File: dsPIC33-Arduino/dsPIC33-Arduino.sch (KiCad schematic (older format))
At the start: 58 parts, among them CON1 BARREL_JACK, P1 Power, P10 PIN20, P11 PIN5, P12 PWR_IN, P13 PIN2, P14 Power Select, P15 I2C, P16 PIN19, P17 UART, P2 Analog, P3 Digital, P4 Digital, P5 CONN_1, P6 CONN_1, P7 CONN_1, P8 CONN_1, P9 USB_B, SW1 SW_PUSH, U1 FT230XS, U2 LM1117 3V3, U3 dsPIC33EVxxxGM102-I/SP, U4 74LVC1G32, U5 7805, Y1 Crystal

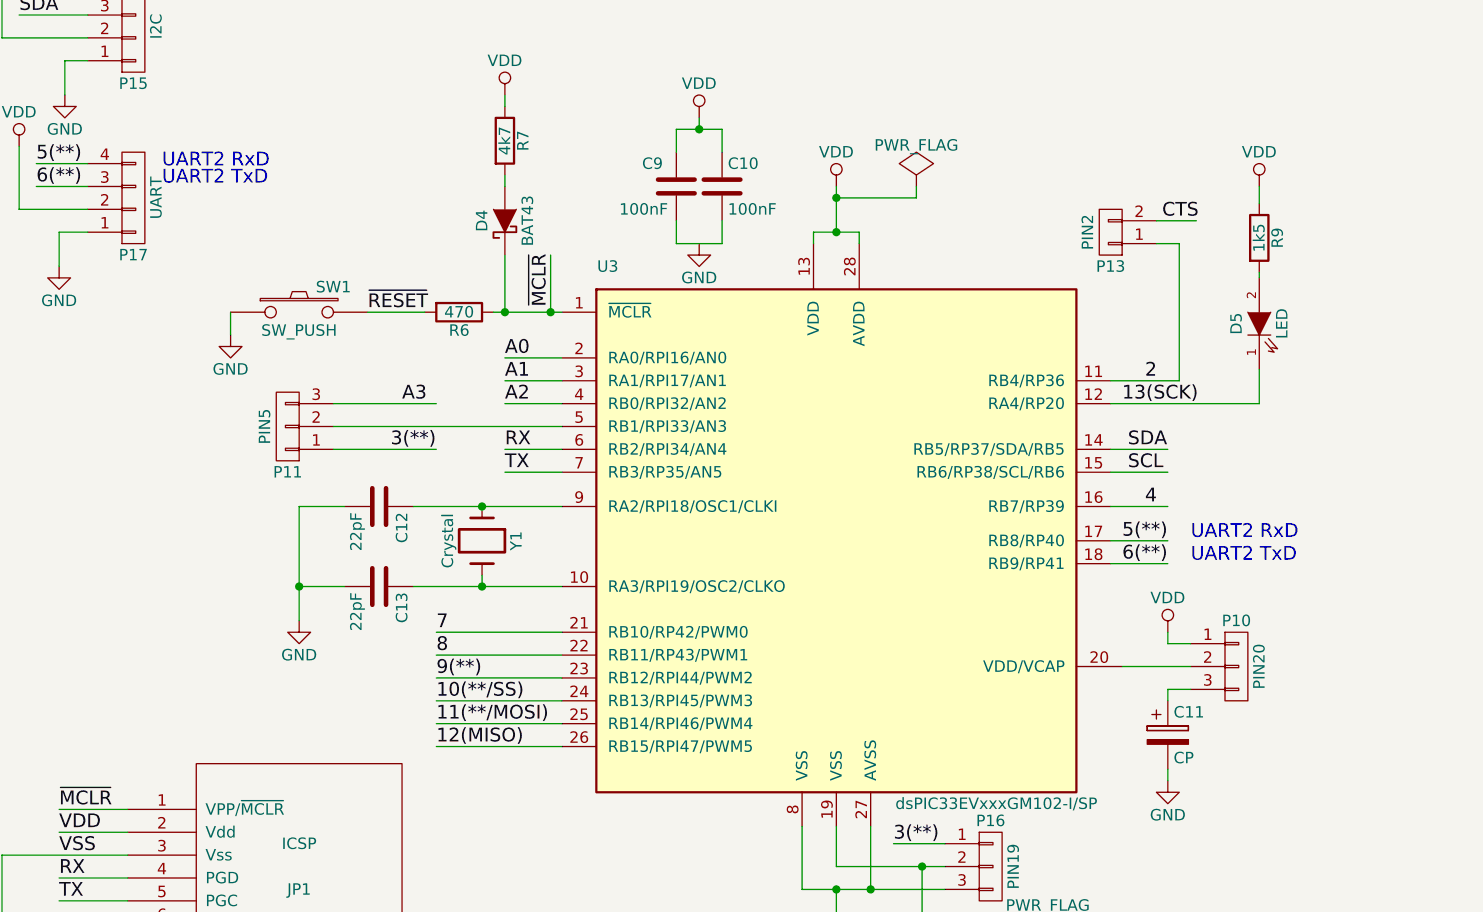
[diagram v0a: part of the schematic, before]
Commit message: use diode the right way
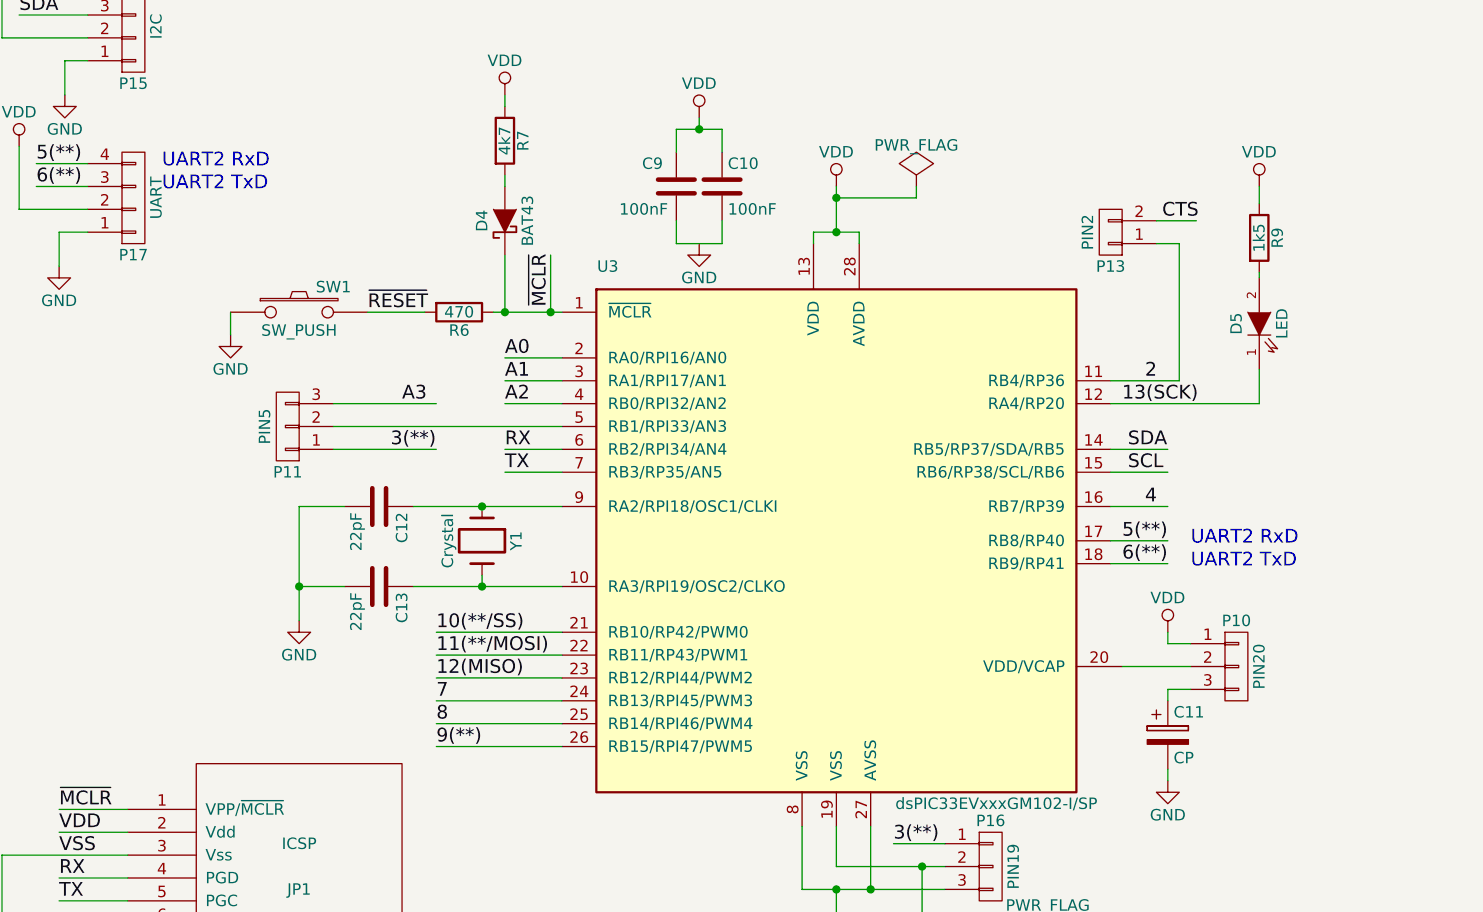
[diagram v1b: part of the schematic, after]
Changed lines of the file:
@@
 Text Label 5550 5800 0    60   ~ 0
 5(**)
+Text Label 2550 6500 0    60   ~ 0
+7
+Text Label 2550 6600 0    60   ~ 0
+8
+Text Label 2550 6700 0    60   ~ 0
+9(**)
 Text Label 2550 6200 0    60   ~ 0
-7
+10(**/SS)
 Text Label 2550 6300 0    60   ~ 0
-8
+11(**/MOSI)
 Text Label 2550 6400 0    60   ~ 0
-9(**)
-Text Label 2550 6500 0    60   ~ 0
-10(**/SS)
-Text Label 2550 6600 0    60   ~ 0
-11(**/MOSI)
-Text Label 2550 6700 0    60   ~ 0
 12(MISO)
 $Comp
@@
 	0    -1   -1   0
 $EndComp
-Text Notes 5850 5900 0    60   ~ 0
+Text Notes 5850 5925 0    60   ~ 0
 UART2 TxD
-Text Notes 5850 5800 0    60   ~ 0
+Text Notes 5850 5825 0    60   ~ 0
 UART2 RxD
-Text Notes 1350 4250 0    60   ~ 0
+Text Notes 1350 4275 0    60   ~ 0
 UART2 TxD
 Text Notes 1350 4175 0    60   ~ 0

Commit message: wip
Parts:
- removed C14, C15, C7: 100nF, Capacitors_ThroughHole:C_Disc_D3_P2.5, symbol C
- added C14, C15, C7: 47uF, w_capacitors:CP_4x5mm, symbol CP
- C11: value CP -> 10uF ESR
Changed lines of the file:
@@
-$EndComp
-$Comp
-L C C7
-U 1 1 588D100F
-P 5650 2700
-F 0 "C7" H 5675 2800 50  0000 L CNN
-F 1 "100nF" H 5675 2600 50  0000 L CNN
-F 2 "Capacitors_ThroughHole:C_Disc_D3_P2.5" H 5688 2550 50  0001 C CNN
-F 3 "" H 5650 2700 50  0000 C CNN
-	1    5650 2700
-	1    0    0    -1
 $EndComp
 $Comp
@@
 P 5750 6650
 F 0 "C11" H 5775 6750 50  0000 L CNN
-F 1 "CP" H 5775 6550 50  0000 L CNN
+F 1 "10uF ESR" H 5775 6550 50  0000 L CNN
 F 2 "w_capacitors:CP_4x5mm" H 5788 6500 50  0001 C CNN
 F 3 "" H 5750 6650 50  0000 C CNN
@@
 F 3 "" H 6100 1850 50  0000 C CNN
 	1    6100 1850
-	1    0    0    -1
-$EndComp
-$Comp
-L C C14
-U 1 1 588E4312
-P 5650 1550
-F 0 "C14" H 5675 1650 50  0000 L CNN
-F 1 "100nF" H 5675 1450 50  0000 L CNN
-F 2 "Capacitors_ThroughHole:C_Disc_D3_P2.5" H 5688 1400 50  0001 C CNN
-F 3 "" H 5650 1550 50  0000 C CNN
-	1    5650 1550
-	1    0    0    -1
-$EndComp
-$Comp
-L C C15
-U 1 1 588E4318
-P 6550 1550
-F 0 "C15" H 6575 1650 50  0000 L CNN
-F 1 "100nF" H 6575 1450 50  0000 L CNN
-F 2 "Capacitors_ThroughHole:C_Disc_D3_P2.5" H 6588 1400 50  0001 C CNN
-F 3 "" H 6550 1550 50  0000 C CNN
-	1    6550 1550
 	1    0    0    -1
 $EndComp
@@
 Text Notes 1350 4175 0    60   ~ 0
 UART2 RxD
+$Comp
+L CP C14
+U 1 1 589DF2D3
+P 5650 1550
+F 0 "C14" H 5675 1650 50  0000 L CNN
+F 1 "47uF" H 5675 1450 50  0000 L CNN
+F 2 "w_capacitors:CP_4x5mm" H 5688 1400 50  0001 C CNN
+F 3 "" H 5650 1550 50  0000 C CNN
+	1    5650 1550
+	1    0    0    -1
+$EndComp
+$Comp
+L CP C15
+U 1 1 589DFD6E
+P 6550 1550
+F 0 "C15" H 6575 1650 50  0000 L CNN
+F 1 "47uF" H 6575 1450 50  0000 L CNN
+F 2 "w_capacitors:CP_4x5mm" H 6588 1400 50  0001 C CNN
+F 3 "" H 6550 1550 50  0000 C CNN
+	1    6550 1550
+	1    0    0    -1
+$EndComp
+$Comp
+L CP C7
+U 1 1 589E0766
+P 5650 2700
+F 0 "C7" H 5675 2800 50  0000 L CNN
+F 1 "47uF" H 5675 2600 50  0000 L CNN
+F 2 "w_capacitors:CP_4x5mm" H 5688 2550 50  0001 C CNN
+F 3 "" H 5650 2700 50  0000 C CNN
+	1    5650 2700
+	1    0    0    -1
+$EndComp
 $EndSCHEMATC

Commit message: V1.0 production
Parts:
- added R11, R12: 3k3, w_pth_resistors:RC03, symbol R
- P2: renamed from P13; value PIN2 -> CTS
- U3: symbol dsPIC33EVxxxGM102-I/SP -> dsPIC33EVxxxGM102-I/SP-RESCUE-dsPIC33-Arduino
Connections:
- wire segments 217 -> 222
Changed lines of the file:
@@
 $EndComp
 $Comp
-L dsPIC33EVxxxGM102-I/SP U3
+L dsPIC33EVxxxGM102-I/SP-RESCUE-dsPIC33-Arduino U3
 U 1 1 588DA463
 P 4300 5800
@@
 Text Label 5650 5100 0    60   ~ 0
 2
-Text Label 2350 5400 0    60   ~ 0
+Text Label 5550 5650 0    60   ~ 0
 3(**)
 $Comp
@@
 Text Label 5550 5200 0    60   ~ 0
 13(SCK)
-Text Label 5650 5650 0    60   ~ 0
+Text Label 2450 5400 0    60   ~ 0
 4
 Text Label 5550 5800 0    60   ~ 0
@@
 $EndComp
 $Comp
-L CONN_01X02 P13
+L CONN_01X02 P2
 U 1 1 588F890F
 P 5500 4450
-F 0 "P13" H 5500 4600 50  0000 C CNN
-F 1 "PIN2" V 5600 4450 50  0000 C CNN
+F 0 "P2" H 5500 4600 50  0000 C CNN
+F 1 "CTS" V 5600 4450 50  0000 C CNN
 F 2 "Pin_Headers:Pin_Header_Straight_1x02" H 5500 4450 50  0001 C CNN
 F 3 "" H 5500 4450 50  0000 C CNN
@@
 	1    0    0    -1
 $EndComp
-Text Label 4550 7125 0    60   ~ 0
-3(**)
 $Comp
 L PWR_FLAG #FLG042
@@
 Connection ~ 2850 4800
 Wire Wire Line
-	5500 5400 5750 5400
-Wire Wire Line
-	5500 5500 5750 5500
+	5500 5400 6375 5400
+Wire Wire Line
+	5500 5500 6475 5500
 Wire Wire Line
 	5500 5800 5750 5800
@@
 	1    0    0    -1
 $EndComp
+Text Label 4550 7125 0    60   ~ 0
+4
+Connection ~ 3700 4500
+$Comp
+L R R11
+U 1 1 589E7364
+P 6375 5250
+F 0 "R11" V 6300 5250 50  0000 C CNN
+F 1 "3k3" V 6375 5250 50  0000 C CNN
+F 2 "w_pth_resistors:RC03" V 6305 5250 50  0001 C CNN
+F 3 "" H 6375 5250 50  0000 C CNN
+	1    6375 5250
+	1    0    0    -1
+$EndComp
+$Comp
+L R R12
+U 1 1 589E75B1
+P 6475 5250
+F 0 "R12" V 6555 5250 50  0000 C CNN
+F 1 "3k3" V 6475 5250 50  0000 C CNN
+F 2 "w_pth_resistors:RC03" V 6405 5250 50  0001 C CNN
+F 3 "" H 6475 5250 50  0000 C CNN
+	1    6475 5250
+	1    0    0    -1
+$EndComp
+$Comp
+L VDD #PWR045
+U 1 1 589E780D
+P 6425 5025
+F 0 "#PWR045" H 6425 4875 50  0001 C CNN
+F 1 "VDD" H 6425 5175 50  0000 C CNN
+F 2 "" H 6425 5025 50  0000 C CNN
+F 3 "" H 6425 5025 50  0000 C CNN
+	1    6425 5025
+	1    0    0    -1
+$EndComp
+Wire Wire Line
+	6375 5100 6375 5075
+Wire Wire Line
+	6375 5075 6475 5075
+Wire Wire Line
+	6475 5075 6475 5100
+Wire Wire Line
+	6425 5025 6425 5075
+Connection ~ 6425 5075
+Wire Wire Line
+	6475 5500 6475 5400
 $EndSCHEMATC
